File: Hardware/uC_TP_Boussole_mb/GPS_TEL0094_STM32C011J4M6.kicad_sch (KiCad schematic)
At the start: 14 parts, among them J3 Conn_01x06, J4 Conn_01x05, SW1 SW_Push_DPDT, SW2 SW_Push, SW3 SW_Push, U1 STM32C011J4Mx

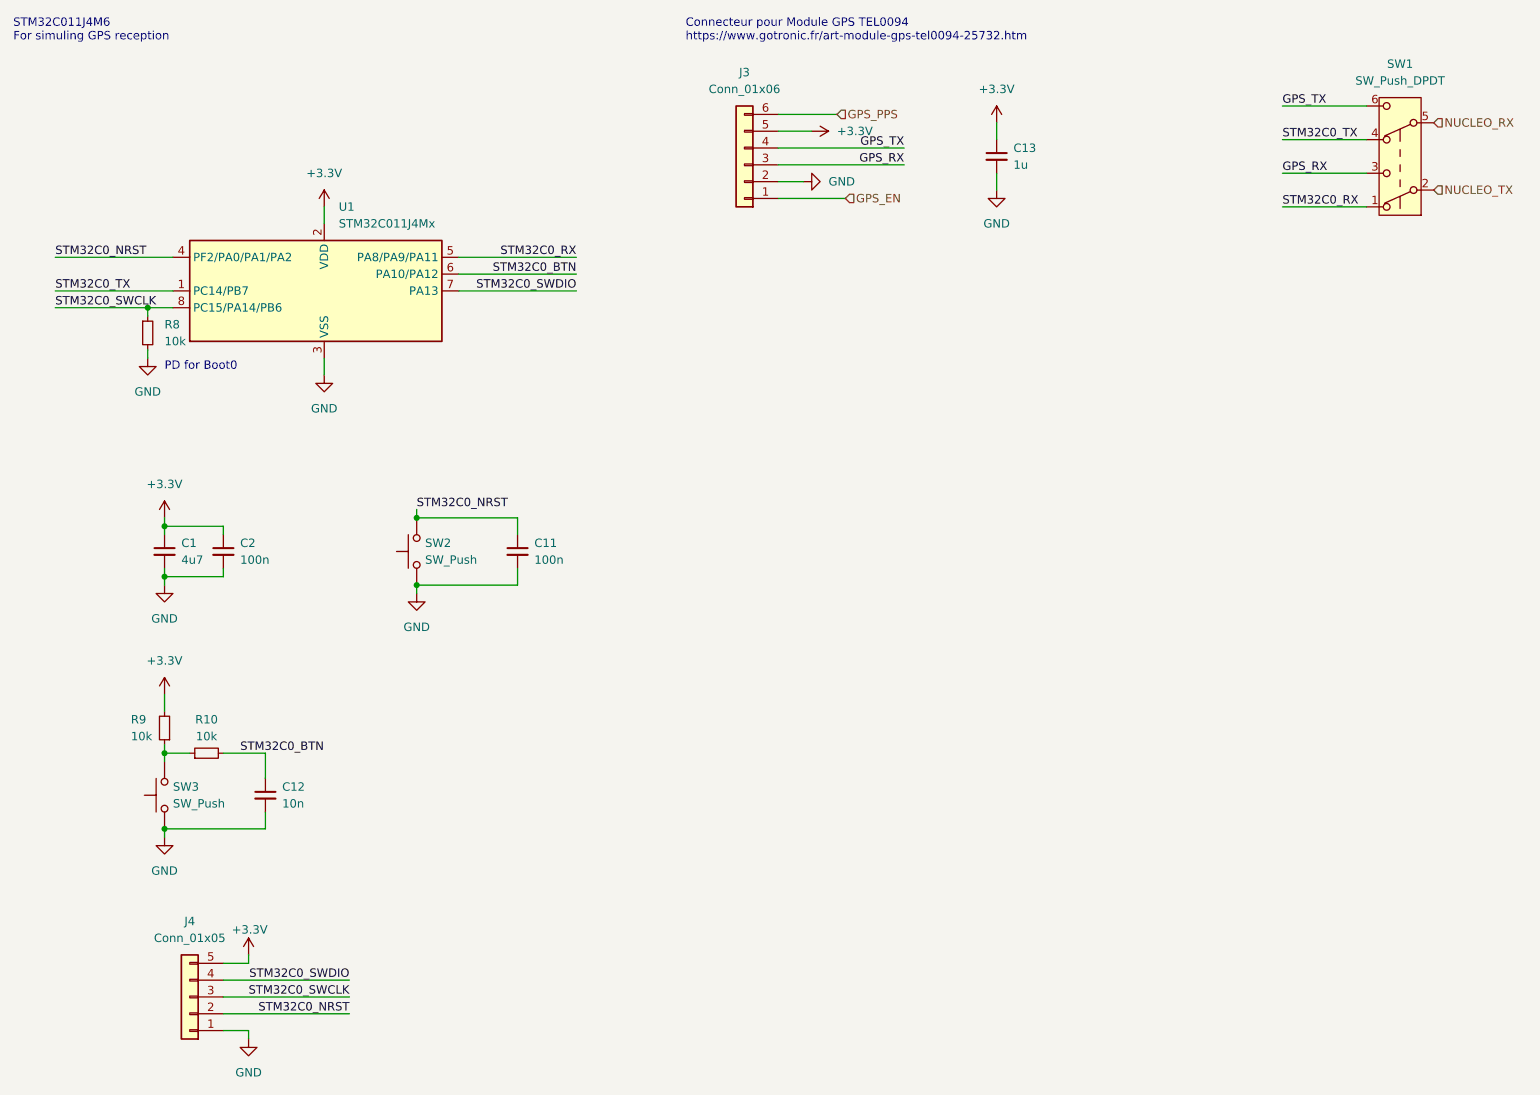
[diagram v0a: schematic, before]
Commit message: starting pin out nucleo
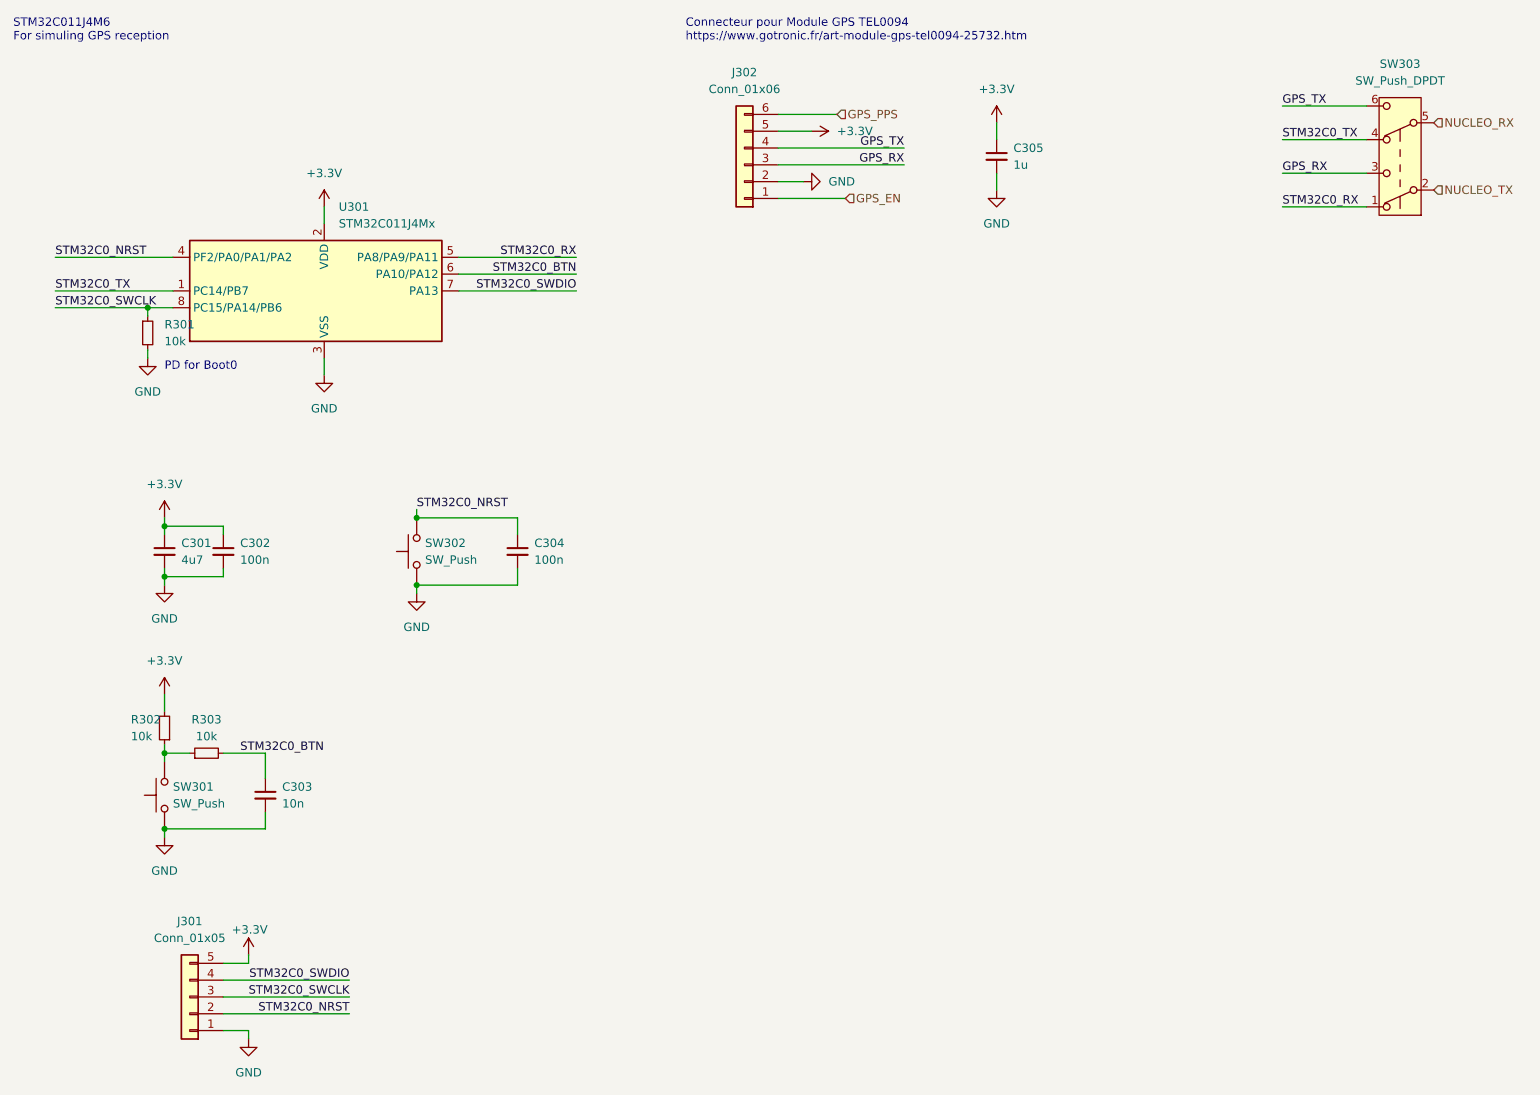
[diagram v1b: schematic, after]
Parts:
- C301: renamed from C1; footprint (none) -> Capacitor_SMD:C_0402_1005Metric
- C302: renamed from C2; footprint (none) -> Capacitor_SMD:C_0402_1005Metric
- C303: renamed from C12; footprint (none) -> Capacitor_SMD:C_0402_1005Metric
- C304: renamed from C11; footprint (none) -> Capacitor_SMD:C_0402_1005Metric
- C305: renamed from C13; footprint (none) -> Capacitor_SMD:C_0402_1005Metric
- J301: renamed from J4; footprint (none) -> Connector_PinHeader_2.54mm:PinHeader_1x05_P2.54mm_Vertical
- J302: renamed from J3; footprint (none) -> Connector_JST:JST_XH_S6B-XH-A_1x06_P2.50mm_Horizontal
- R301: renamed from R8; footprint (none) -> Resistor_SMD:R_0402_1005Metric
- R302: renamed from R9; footprint (none) -> Resistor_SMD:R_0402_1005Metric
- R303: renamed from R10; footprint (none) -> Resistor_SMD:R_0402_1005Metric
- SW301: renamed from SW3; footprint (none) -> Button_Switch_SMD:SW_Push_1P1T_NO_6x6mm_H9.5mm
- SW302: renamed from SW2; footprint (none) -> Button_Switch_SMD:SW_Push_1P1T_NO_6x6mm_H9.5mm
- SW303: renamed from SW1; footprint (none) -> Button_Switch_SMD:SW_DPDT_CK_JS202011JCQN
- renumbered U1 to U301

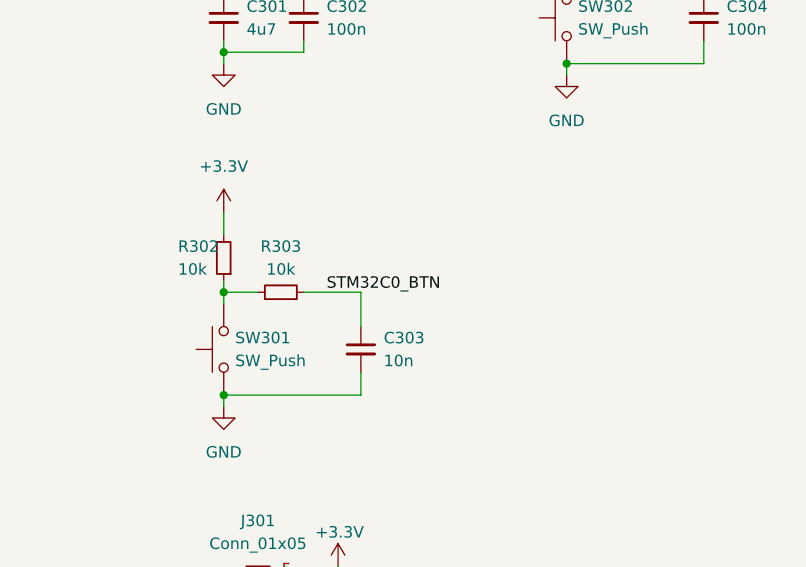
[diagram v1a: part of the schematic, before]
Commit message: update schematic
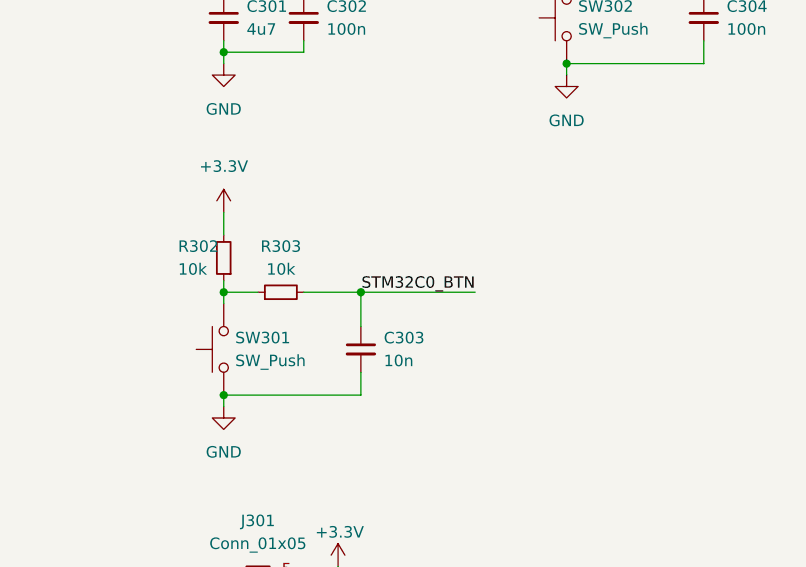
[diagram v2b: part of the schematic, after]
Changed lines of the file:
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@@
+	)
+	(junction
+		(at 63.5 134.62)
+		(diameter 0)
+		(color 0 0 0 0)
 	)
 	(junction
@@
 	(wire
 		(pts
+			(xy 57.15 134.62) (xy 63.5 134.62)
+		)
+		(stroke
+			(width 0)
+			(type default)
+		)
+	)
+	(wire
+		(pts
 			(xy 140.97 48.26) (xy 144.78 48.26)
 		)
@@
 	(wire
 		(pts
-			(xy 57.15 134.62) (xy 63.5 134.62)
-		)
-		(stroke
-			(width 0)
-			(type default)
-		)
-	)
-	(wire
-		(pts
 			(xy 48.26 100.33) (xy 48.26 101.6)
+		)
+		(stroke
+			(width 0)
+			(type default)
+		)
+	)
+	(wire
+		(pts
+			(xy 76.2 134.62) (xy 63.5 134.62)
 		)
 		(stroke
@@
 	)
 	(label "STM32C0_BTN"
-		(at 59.69 134.62 0)
-		(fields_autoplaced yes)
-		(effects
-			(font
-				(size 1.27 1.27)
-			)
-			(justify left bottom)
-		)
-	)
+		(at 76.2 134.62 180)
+		(fields_autoplaced yes)
+		(effects
+			(font
+				(size 1.27 1.27)
+			)
+			(justify right bottom)
+		)
+	)

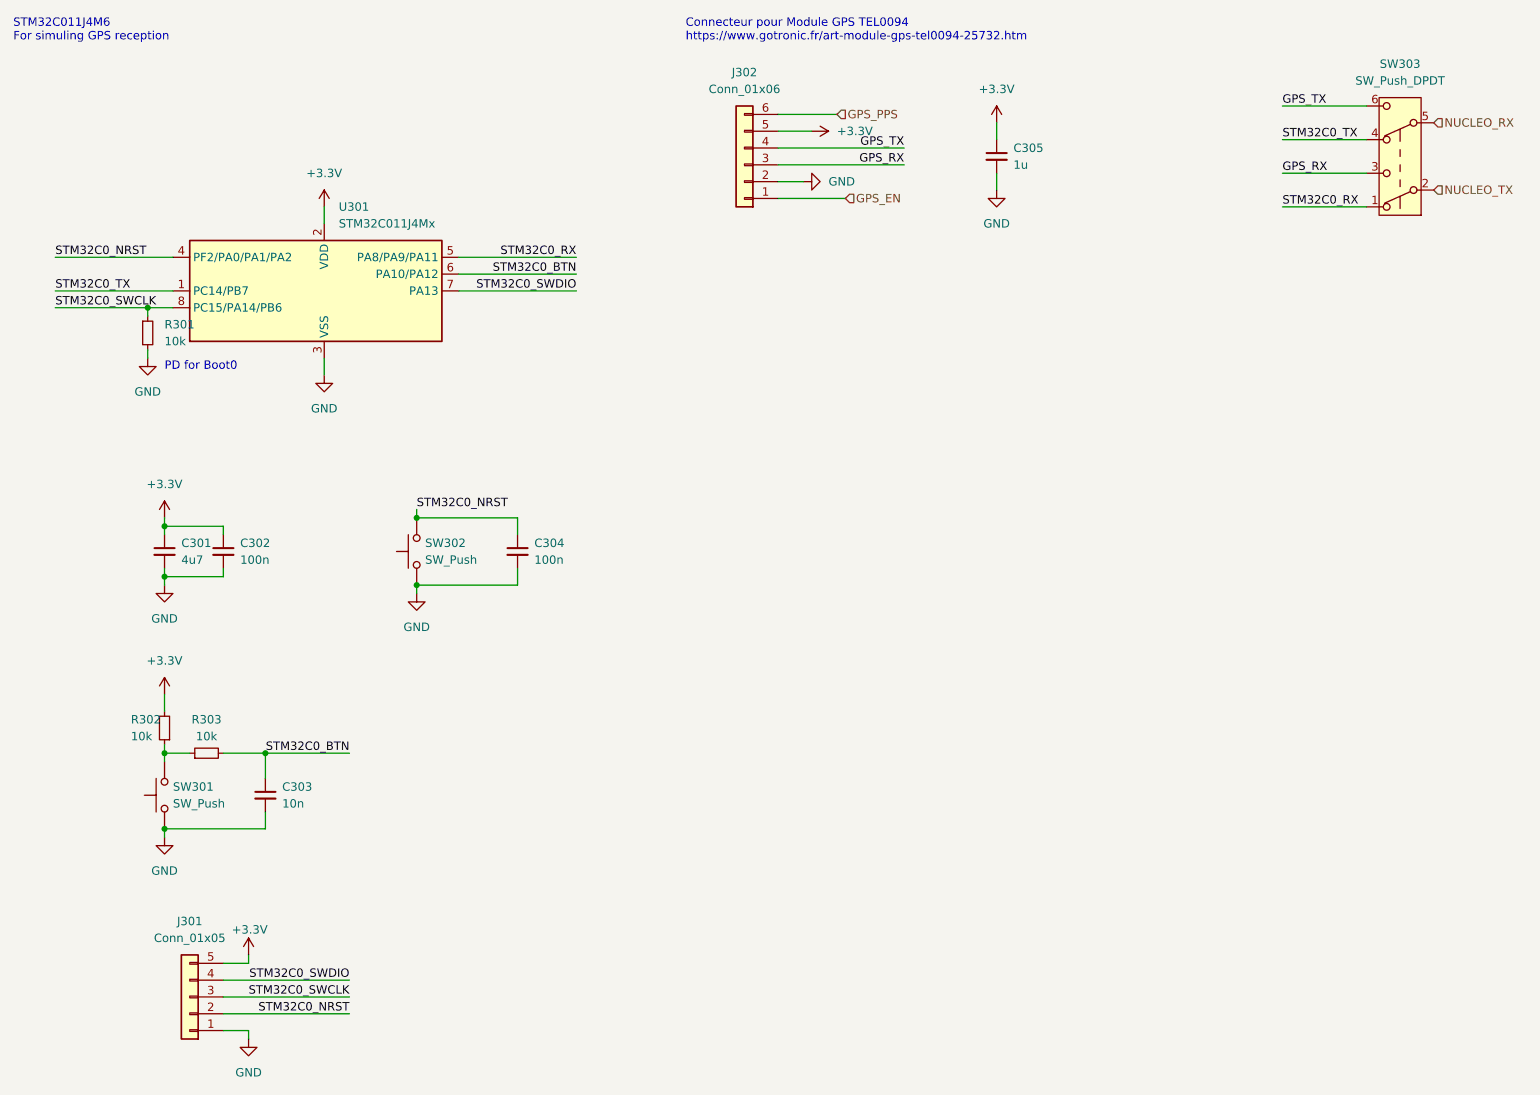
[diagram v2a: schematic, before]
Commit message: update schematic
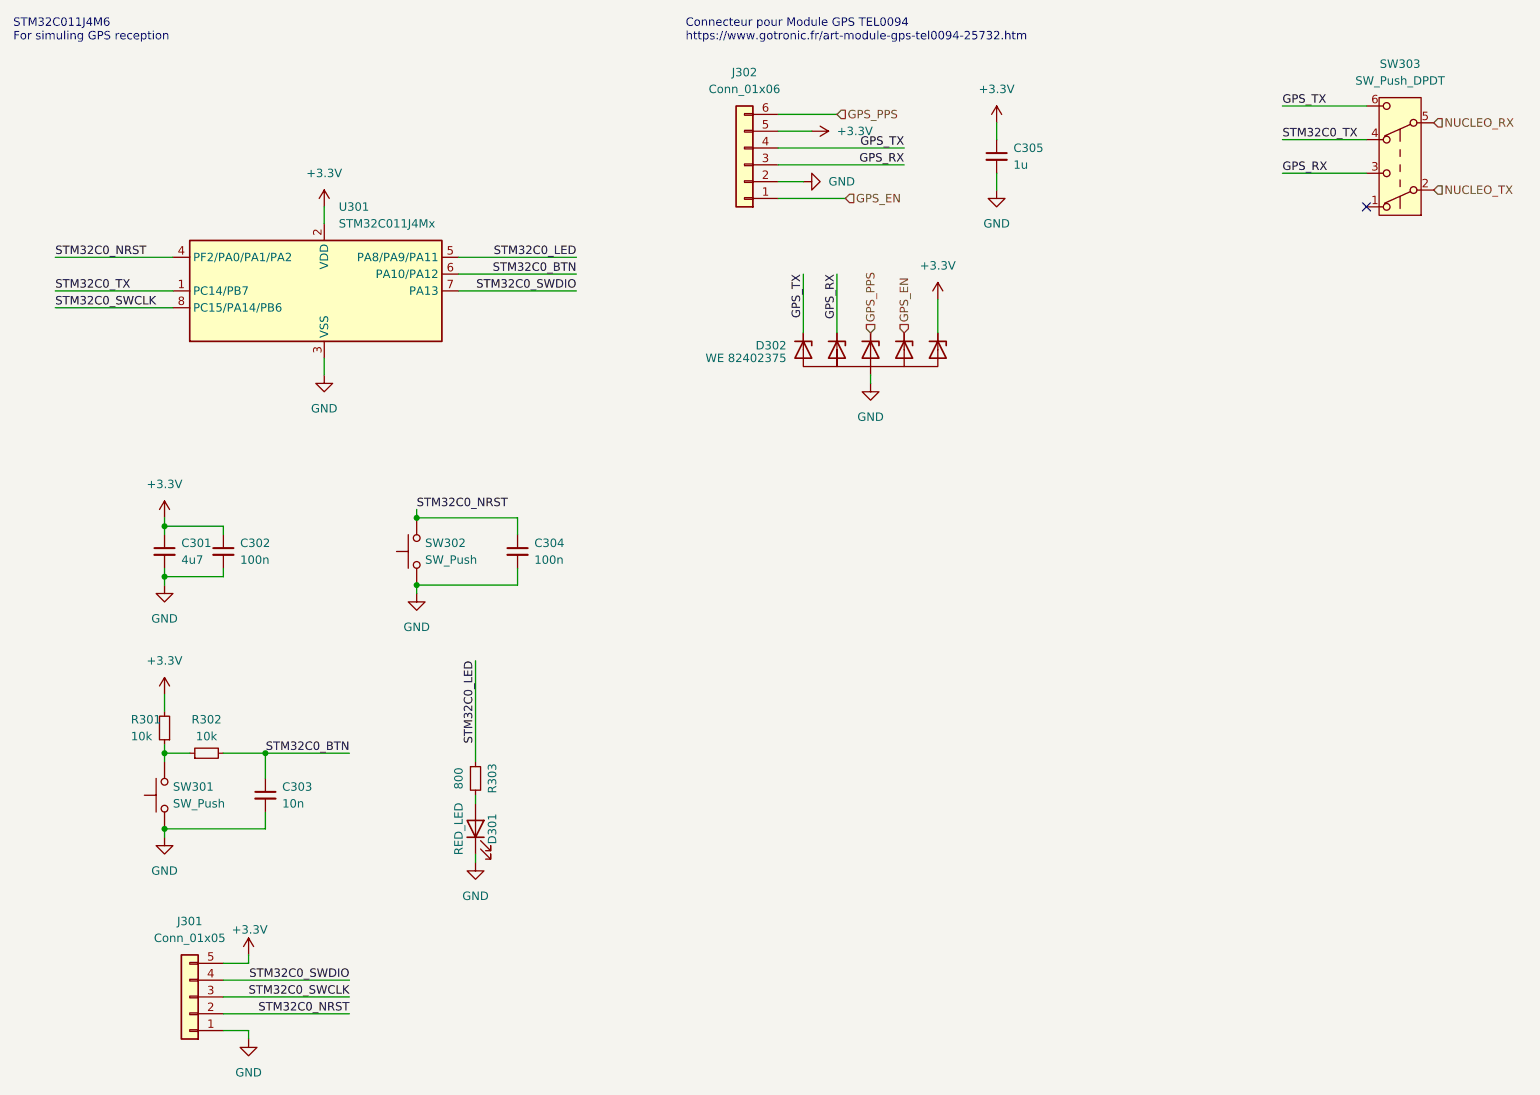
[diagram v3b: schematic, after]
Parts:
- removed R301: 10k, Resistor_SMD:R_0402_1005Metric, symbol Device:R_Small
- added D301: RED_LED, LED_SMD:LED_0603_1608Metric, symbol Device:LED
- added D302: WE 82402375, libs:SC70-6L, symbol mylibs:D_TVS_Uni_x5
- added R303: 800, Resistor_SMD:R_0402_1005Metric, symbol Device:R_Small
- renumbered R302 to R301, R303 to R302
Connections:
- net +3.3V: now also D302.1 (I/O)
- net GND: now also D301.1 (K), D302.2 (GND)
- net GPS_EN: now also D302.3 (I/O)
- net GPS_PPS: now also D302.4 (I/O)
- net GPS_RX: now also D302.5 (I/O)
- net GPS_TX: now also D302.6 (I/O)
- net STM32C0_RX: no longer names the net of SW303.1 (A)
- net STM32C0_RX: no longer U301.5 (PA8/PA9/PA11)
- new net: D301.2 (A), R303.2
- new net STM32C0_LED: R303.1, U301.5 (PA8/PA9/PA11)
- no-connect marks 0 -> 1
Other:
- note removed: "PD for Boot0"

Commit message: finalize pcb
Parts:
- J301: footprint Connector_PinHeader_2.54mm:PinHeader_1x05_P2.54mm_Vertical -> Connector_PinHeader_2.54mm:PinHeader_1x05_P2.54mm_Horizontal
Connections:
- net GPS_EN: now also D302.4 (I/O); no longer D302.3 (I/O)
- net GPS_PPS: now also D302.3 (I/O); no longer D302.4 (I/O)
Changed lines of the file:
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@@
+		)
+	)
+	(hierarchical_label "GPS_PPS"
+		(shape input)
+		(at 160.02 71.12 90)
+		(fields_autoplaced yes)
+		(effects
+			(font
+				(size 1.27 1.27)
+			)
+			(justify left)
 		)
 	)
@@
 	(hierarchical_label "GPS_EN"
 		(shape input)
-		(at 160.02 71.12 90)
+		(at 151.13 50.8 0)
 		(fields_autoplaced yes)
 		(effects
@@
 		)
 	)
-	(hierarchical_label "GPS_PPS"
+	(hierarchical_label "GPS_EN"
 		(shape input)
 		(at 154.94 71.12 90)
@@
 		)
 	)
-	(hierarchical_label "GPS_EN"
-		(shape input)
-		(at 151.13 50.8 0)
-		(fields_autoplaced yes)
-		(effects
-			(font
-				(size 1.27 1.27)
-			)
-			(justify left)
-		)
-	)
 	(symbol
 		(lib_id "Device:C_Small")
@@
 			)
 		)
-		(property "Footprint" "Connector_PinHeader_2.54mm:PinHeader_1x05_P2.54mm_Vertical"
+		(property "Footprint" "Connector_PinHeader_2.54mm:PinHeader_1x05_P2.54mm_Horizontal"
 			(at 52.07 171.45 0)
 			(effects

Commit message: create BOM, update MPN
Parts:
- SW301, SW302: MPN (none) -> 430182070816
- SW303: MPN (none) -> JS202011JCQN
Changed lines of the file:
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@@
+			)
+		)
+		(property "MPN" "JS202011JCQN"
+			(at 234.95 44.45 0)
+			(effects
+				(font
+					(size 1.27 1.27)
+				)
+				(hide yes)
 			)
 		)
@@
 			)
 		)
+		(property "MPN" "430182070816"
+			(at 48.26 140.97 90)
+			(effects
+				(font
+					(size 1.27 1.27)
+				)
+				(hide yes)
+			)
+		)
 		(pin "2"
 		)
@@
 			(effects
 				(font
+					(size 1.27 1.27)
+				)
+				(hide yes)
+			)
+		)
+		(property "MPN" "430182070816"
+			(at 86.36 104.14 90)
+			(effects
+				(font

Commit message: bom
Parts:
- D301: MPN 150060RS55040 -> WE 150060RS55040
- SW301, SW302: MPN 430182070816 -> WE 430182070816
- U301: MPN (none) -> STM32C011J4M6
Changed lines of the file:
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@@
 			)
 		)
-		(property "MPN" "150060RS55040"
+		(property "MPN" "WE 150060RS55040"
 			(at 95.25 146.05 0)
 			(effects
@@
 			)
 		)
+		(property "MPN" "STM32C011J4M6"
+			(at 69.85 64.77 0)
+			(effects
+				(font
+					(size 1.27 1.27)
+				)
+				(hide yes)
+			)
+		)
 		(pin "6"
 		)
@@
 			)
 		)
-		(property "MPN" "430182070816"
+		(property "MPN" "WE 430182070816"
 			(at 48.26 140.97 90)
 			(effects
@@
 			)
 		)
-		(property "MPN" "430182070816"
+		(property "MPN" "WE 430182070816"
 			(at 86.36 104.14 90)
 			(effects
